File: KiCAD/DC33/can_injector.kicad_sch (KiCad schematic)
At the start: 27 parts, among them U17 ADG849YKSZ-REEL, U19 ADG849YKSZ-REEL, U21 ALM2403QPWPRQ1, U22 TMUX1108PWR, U24 TMUX1108PWR, U27 TPS22810TDBVRQ1

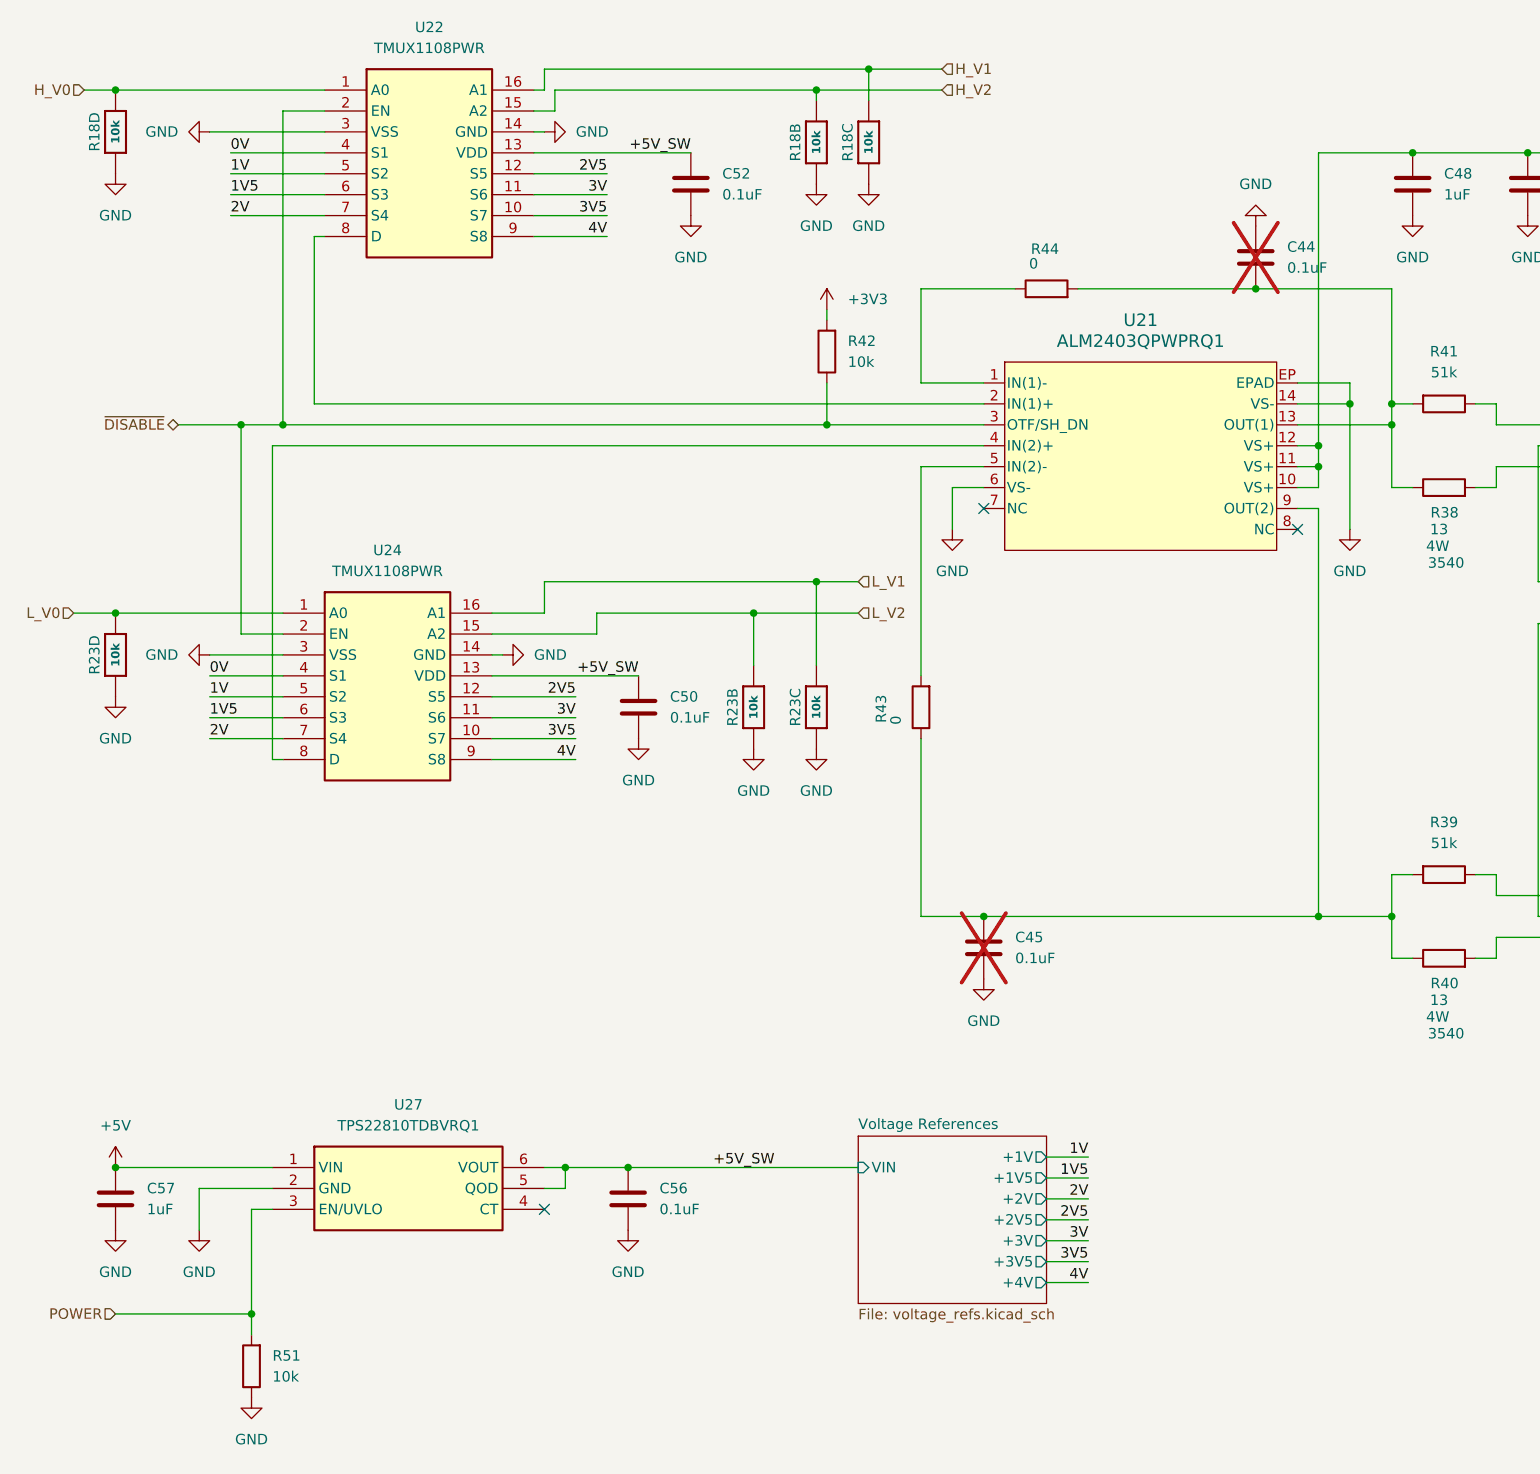
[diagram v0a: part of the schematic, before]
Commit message: refactor(schematic): change DAC from switches to R-2R DAC)
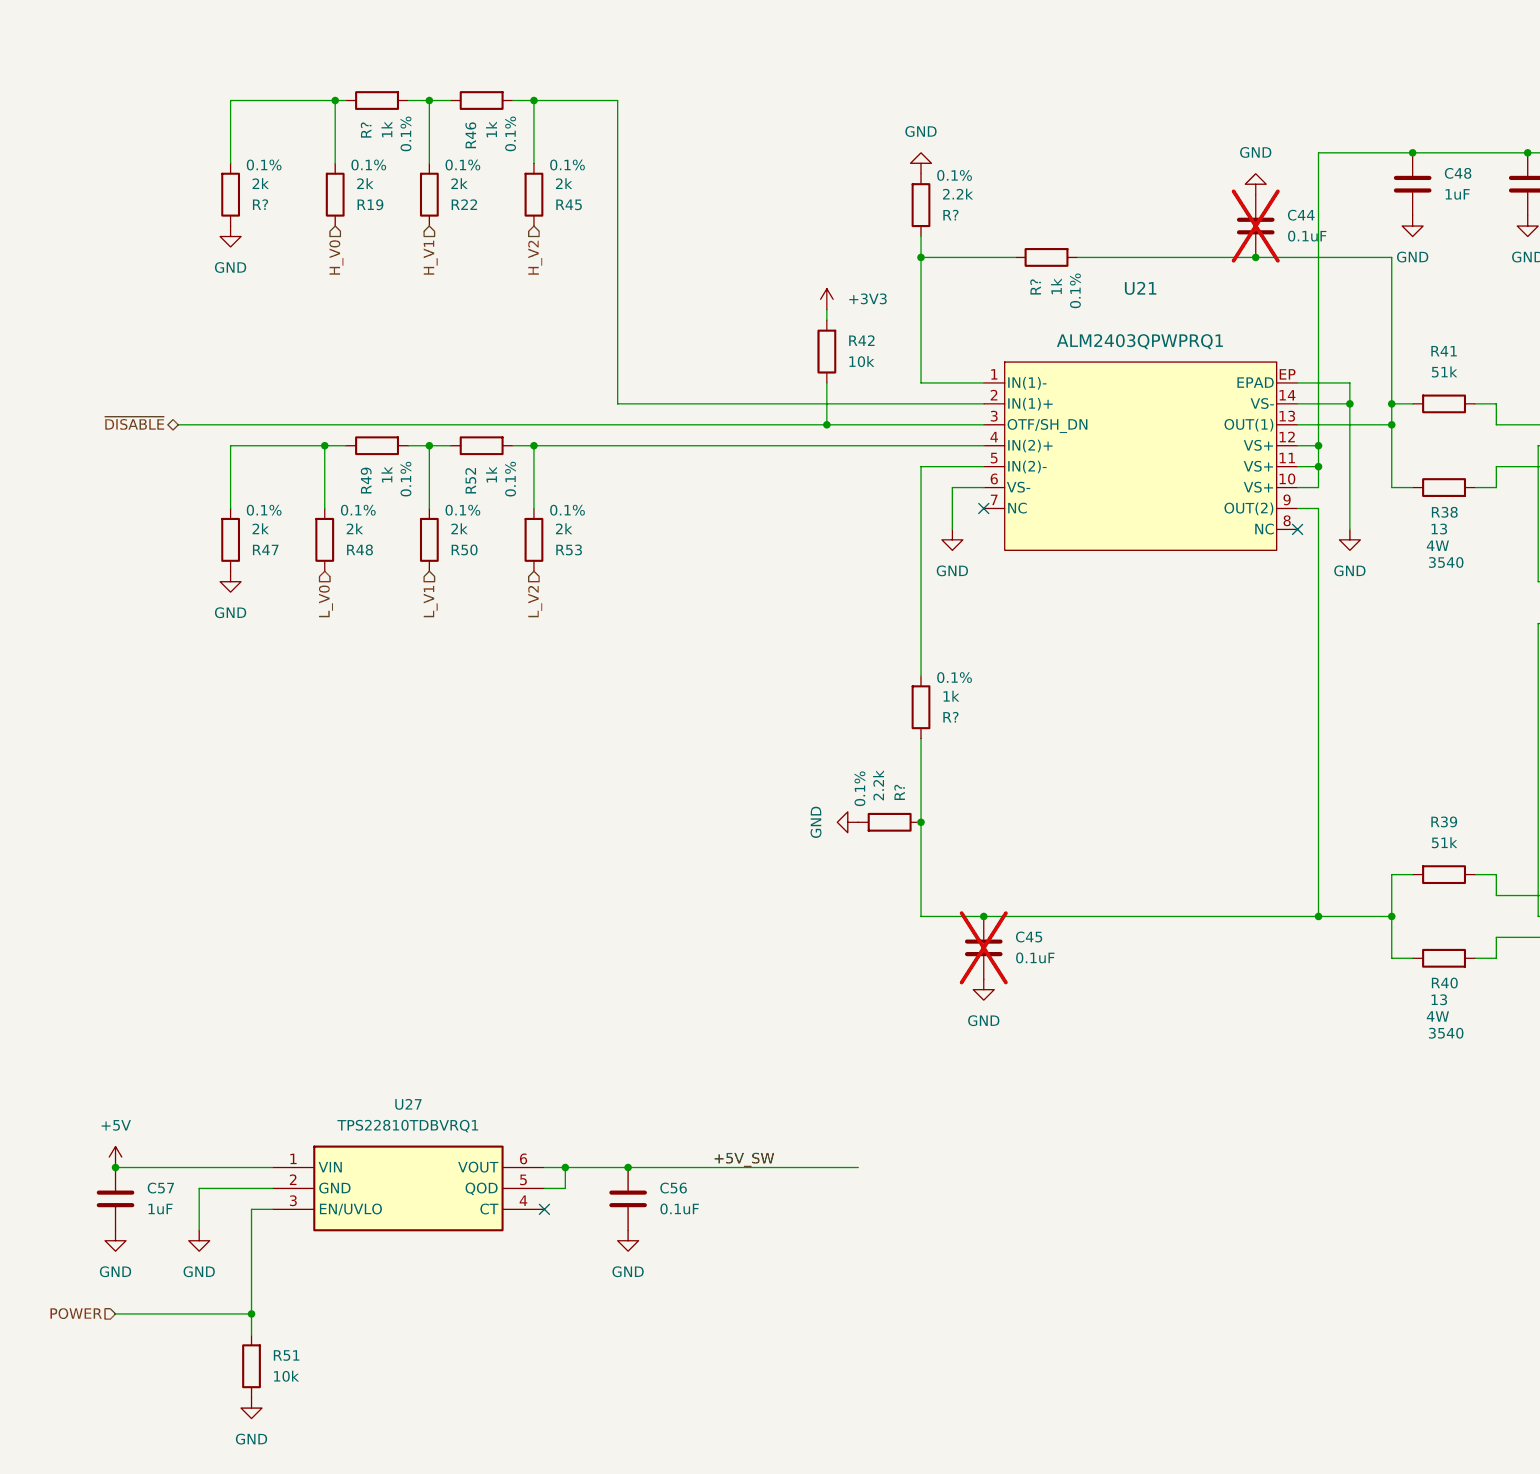
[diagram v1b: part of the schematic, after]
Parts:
- removed C50, C52: 0.1uF, Capacitor_SMD:C_0603_1608Metric, symbol Library:C
- removed unit 3 of R18
- removed unit 4 of R18
- removed unit 2 of R18
- removed unit 3 of R23
- removed unit 2 of R23
- removed unit 4 of R23
- removed R43, R44: 0, Resistor_SMD:R_0603_1608Metric, symbol Library:R
- removed U22, U24: TMUX1108PWR, Library:SOP65P640X120-16N, symbol Library:TMUX1108PWR
- added R19, R22, R45, R47, R48, R50, R53, R?: 2k, Resistor_SMD:R_0603_1608Metric, symbol Library:R
- added R46, R49, R52, R? (x3): 1k, Resistor_SMD:R_0603_1608Metric, symbol Library:R
- added R? (x2): 2.2k, Resistor_SMD:R_0603_1608Metric, symbol Library:R
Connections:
- net GND: now also R47.1, R?.1, R?.2, R?.2
- net H_V0: now also R19.1
- net H_V1: now also R22.1
- net H_V2: now also R45.1
- net L_V0: now also R48.1
- net L_V1: now also R50.1
- net L_V2: now also R53.1
- net at C45.1, R39.2, R40.1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: now also R?.1, R?.1
- net at U21.5 (IN(2)-): now also R?.2
- net at U21.4 (IN(2)+): now also R52.2, R53.2
- net at C44.2, R38.1, R41.2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: now also R?.2
- net at U21.1 (IN(1)-): now also R?.1, R?.1
- net at U21.2 (IN(1)+): now also R45.2, R46.2
- new net: R49.2, R50.2, R52.1
- new net: R47.2, R48.2, R49.1
- new net: R19.2, R?.1, R?.2
- new net: R22.2, R46.1, R?.2
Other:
- removed sheet Voltage References
- moved on the sheet: C44

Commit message: render
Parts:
- gave numbers to parts that had none: 6
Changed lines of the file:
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@@
 		(in_pos_files yes)
 		(dnp no)
-		(property "Reference" "R?"
+		(property "Reference" "R56"
 			(at 128.27 102.8701 0)
 			(show_name no)
@@
 			(project "DC33"
 				(path "/c031bbd5-e288-461b-abff-d4e8c5230266/e1398a93-5b5e-4ef8-b70c-1732cdecb585"
-					(reference "R?")
+					(reference "R56")
 					(unit 1)
 				)
@@
 		(in_pos_files yes)
 		(dnp no)
-		(property "Reference" "R?"
+		(property "Reference" "R43"
 			(at 44.45 40.6401 0)
 			(show_name no)
@@
 			(project "DC33"
 				(path "/c031bbd5-e288-461b-abff-d4e8c5230266/e1398a93-5b5e-4ef8-b70c-1732cdecb585"
-					(reference "R?")
+					(reference "R43")
 					(unit 1)
 				)
@@
 		(in_pos_files yes)
 		(dnp no)
-		(property "Reference" "R?"
+		(property "Reference" "R55"
 			(at 128.27 41.9101 0)
 			(show_name no)
@@
 			(project "DC33"
 				(path "/c031bbd5-e288-461b-abff-d4e8c5230266/e1398a93-5b5e-4ef8-b70c-1732cdecb585"
-					(reference "R?")
+					(reference "R55")
 					(unit 1)
 				)
@@
 		(in_pos_files yes)
 		(dnp no)
-		(property "Reference" "R?"
+		(property "Reference" "R44"
 			(at 58.4199 30.48 0)
 			(show_name no)
@@
 			(project "DC33"
 				(path "/c031bbd5-e288-461b-abff-d4e8c5230266/e1398a93-5b5e-4ef8-b70c-1732cdecb585"
-					(reference "R?")
+					(reference "R44")
 					(unit 1)
 				)
@@
 		(in_pos_files yes)
 		(dnp no)
-		(property "Reference" "R?"
+		(property "Reference" "R54"
 			(at 123.1901 113.03 0)
 			(show_name no)
@@
 			(project "DC33"
 				(path "/c031bbd5-e288-461b-abff-d4e8c5230266/e1398a93-5b5e-4ef8-b70c-1732cdecb585"
-					(reference "R?")
+					(reference "R54")
 					(unit 1)
 				)
@@
 		(in_pos_files yes)
 		(dnp no)
-		(property "Reference" "R?"
+		(property "Reference" "R57"
 			(at 139.6999 49.53 0)
 			(show_name no)
@@
 			(project "DC33"
 				(path "/c031bbd5-e288-461b-abff-d4e8c5230266/e1398a93-5b5e-4ef8-b70c-1732cdecb585"
-					(reference "R?")
+					(reference "R57")
 					(unit 1)
 				)
